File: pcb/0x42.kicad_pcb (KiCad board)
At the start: 2 copper layers, 285 x 95.1 mm, 196 parts, among them J1 USB_C_Receptacle_USB2.0, J2 Conn_01x04, J3 SWD, K000 1.5U, K001 1U, K002 1U, K003 1U, K004 1U, K005 1U, K006 1U, K007 1U, K008 1U, K009 1U, K010 1U, K011 1U, K012 1U, K013 1.5U, K100 1.5U, K101 1U, K102 1U, K103 1U, K104 1U, K105 1U, K106 1U, K107 1U, K108 1U, K109 1U, K110 1U, K111 1U, K112 1U, K113 1.5U, K200 1.5U, K201 1U, K202 1U, K203 1U, K204 1U, K205 1U, K206 1U, K207 1U, K208 1U, K209 1U, K210 1U, K211 1U, K212 1U, K213 1.5U, K300 1.5U, K301 1U, K302 1U, K303 1U, K304 1U, K305 1U, K306 1U, K307 1U, K308 1U, K309 1U, K310 1U, K311 1U, K312 1U, K313 1.5U, K400 1.5U, K401 1U, K402 1U, K403 1U, K404 1U, K405 1U, K406 1U, K407 1U, K408 1U, K409 1U, K410 1U, K411 1U, K412 1U, K413 1.5U, SW1 Reset, SW2 Boot, U1 STM32F072CBUx, U2 MCP1700-3302E_SOT89, U3 IS31FL3731-QF

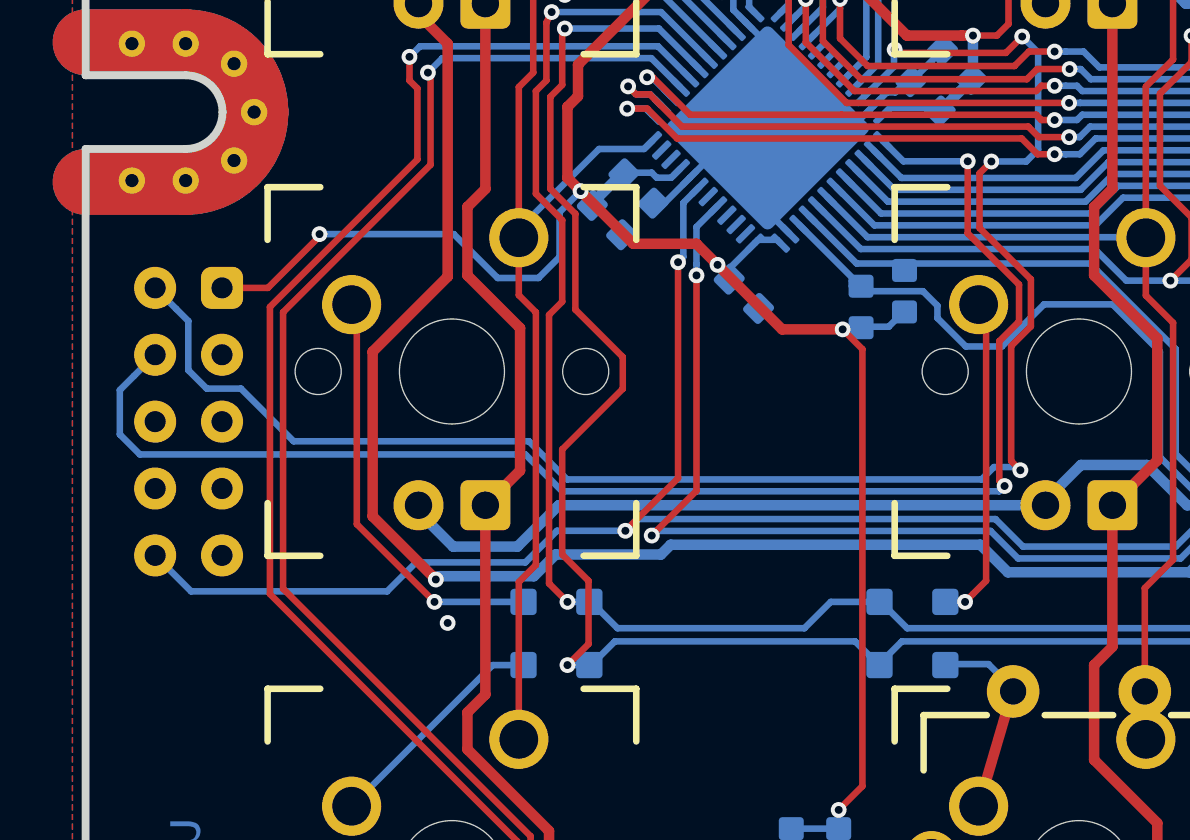
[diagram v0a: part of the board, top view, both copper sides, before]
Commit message: Replace 2x05pins SWD connector by 1x06 (Nucleo CN4 pinout)
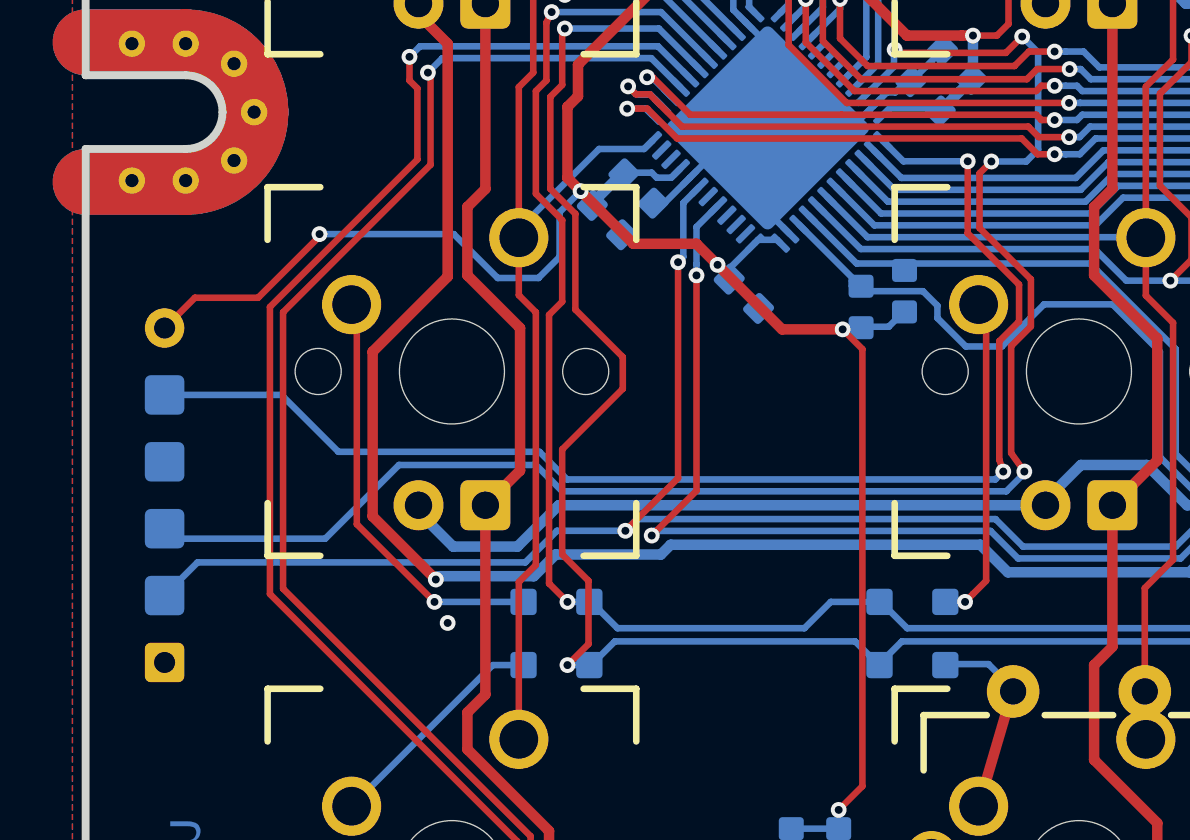
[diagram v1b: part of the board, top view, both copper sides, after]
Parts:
- J3: value SWD -> SWD_CN4; footprint 0xLib_STM32:ARM_JTAG_SWD_10 -> 0xLib_STM32:SWD_1x06_P2.54mm_POGO
- moved J3 8.17 mm to (72.5, 139.8)
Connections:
- J3 pad 2: SWDIO -> SWDCLK
- J3 pad 4: SWDCLK -> SWDIO
- J3 pad 5: GND -> NRST
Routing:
- net SWDCLK: track 55.4 -> 50.0 mm
- net +3V3: track 136.8 -> 139.6 mm
- net SWDIO: track 64.3 -> 61.9 mm
- net NRST: track 98.3 -> 97.4 mm
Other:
- board text added: "Hold Boot during Reset to enter DFU booloader mode"
- board text removed: "Hold Boot during Reset to start in DFU booloader mode"
